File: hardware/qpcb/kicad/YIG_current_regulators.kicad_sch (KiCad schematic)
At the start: 19 parts, among them IC12 DAC8562TDGSR, J16 Conn_01x04, J17 Conn_01x04, Q7 NPN, Q8 NPN, U21 LT1632CS8#PBF, U22 LT1632CS8#PBF

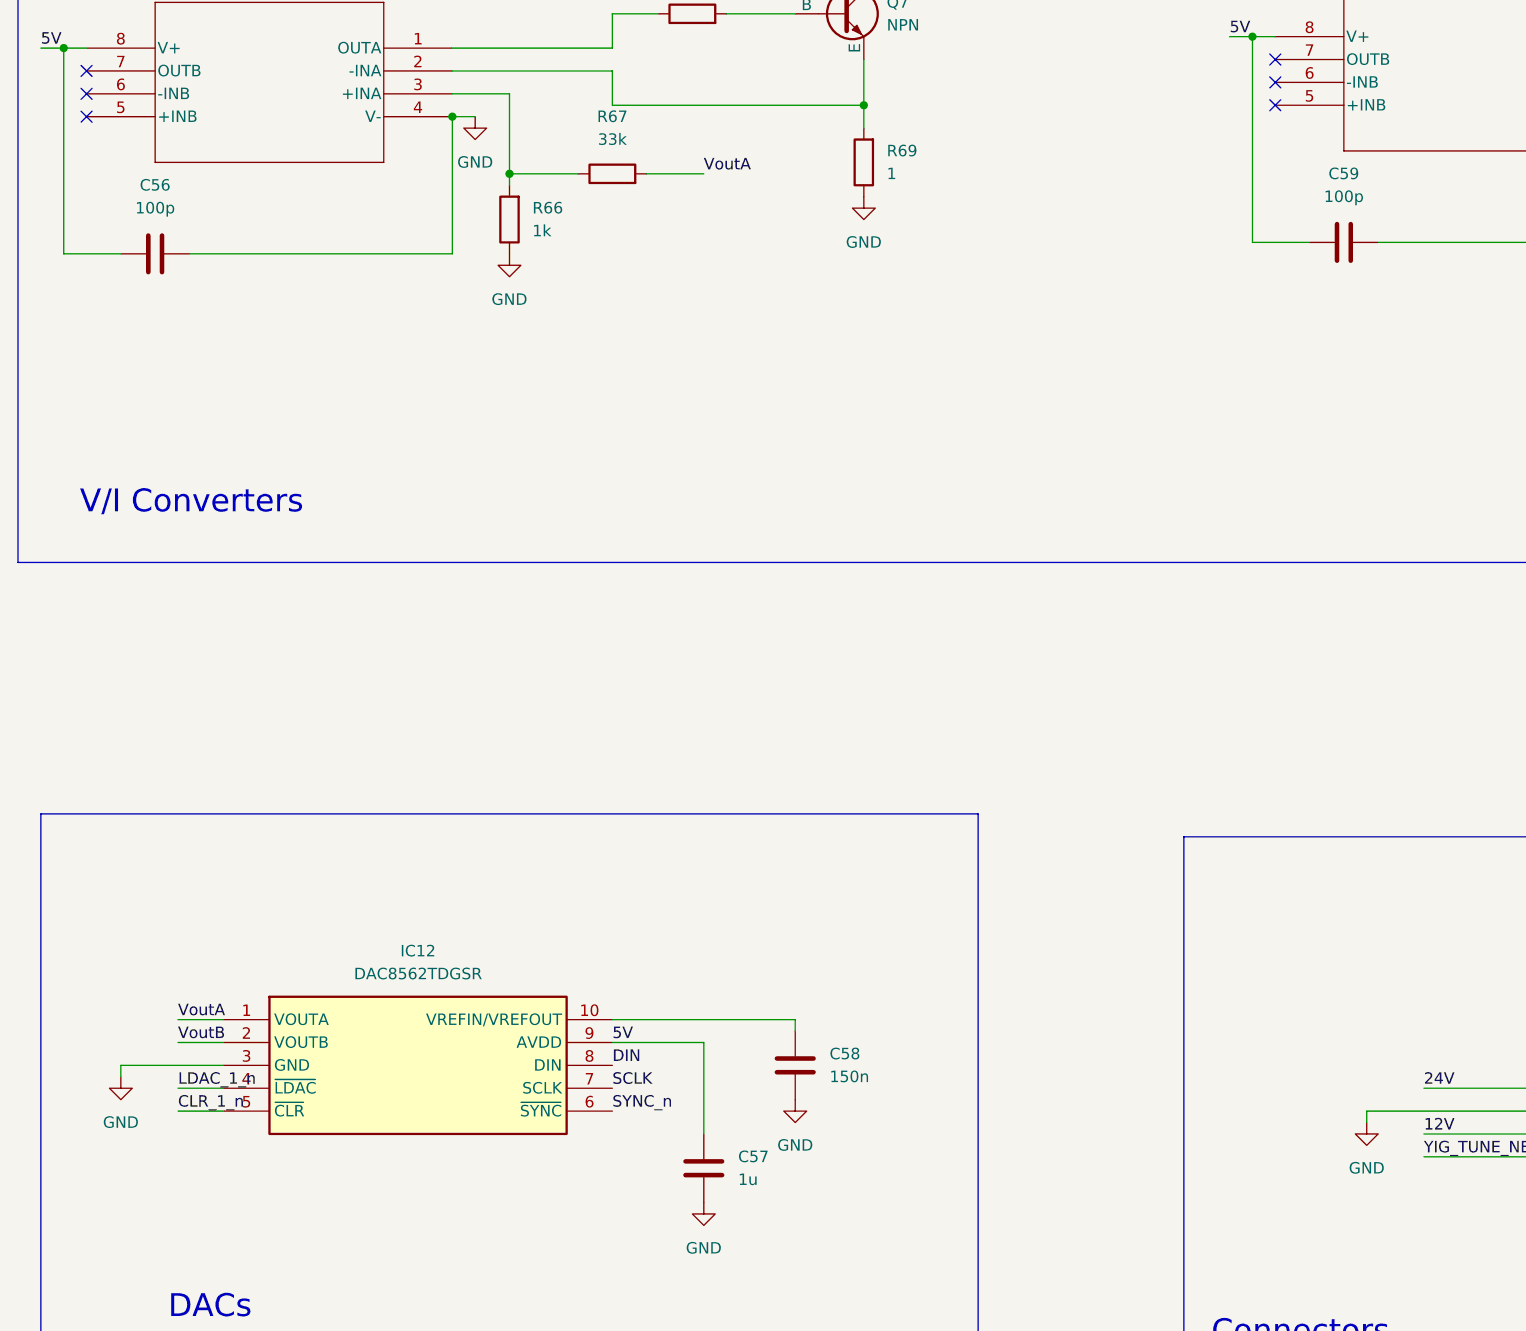
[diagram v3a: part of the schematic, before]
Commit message: Add final footprints of daughter boards, change components for -3v3 power supply line and placement almost finished
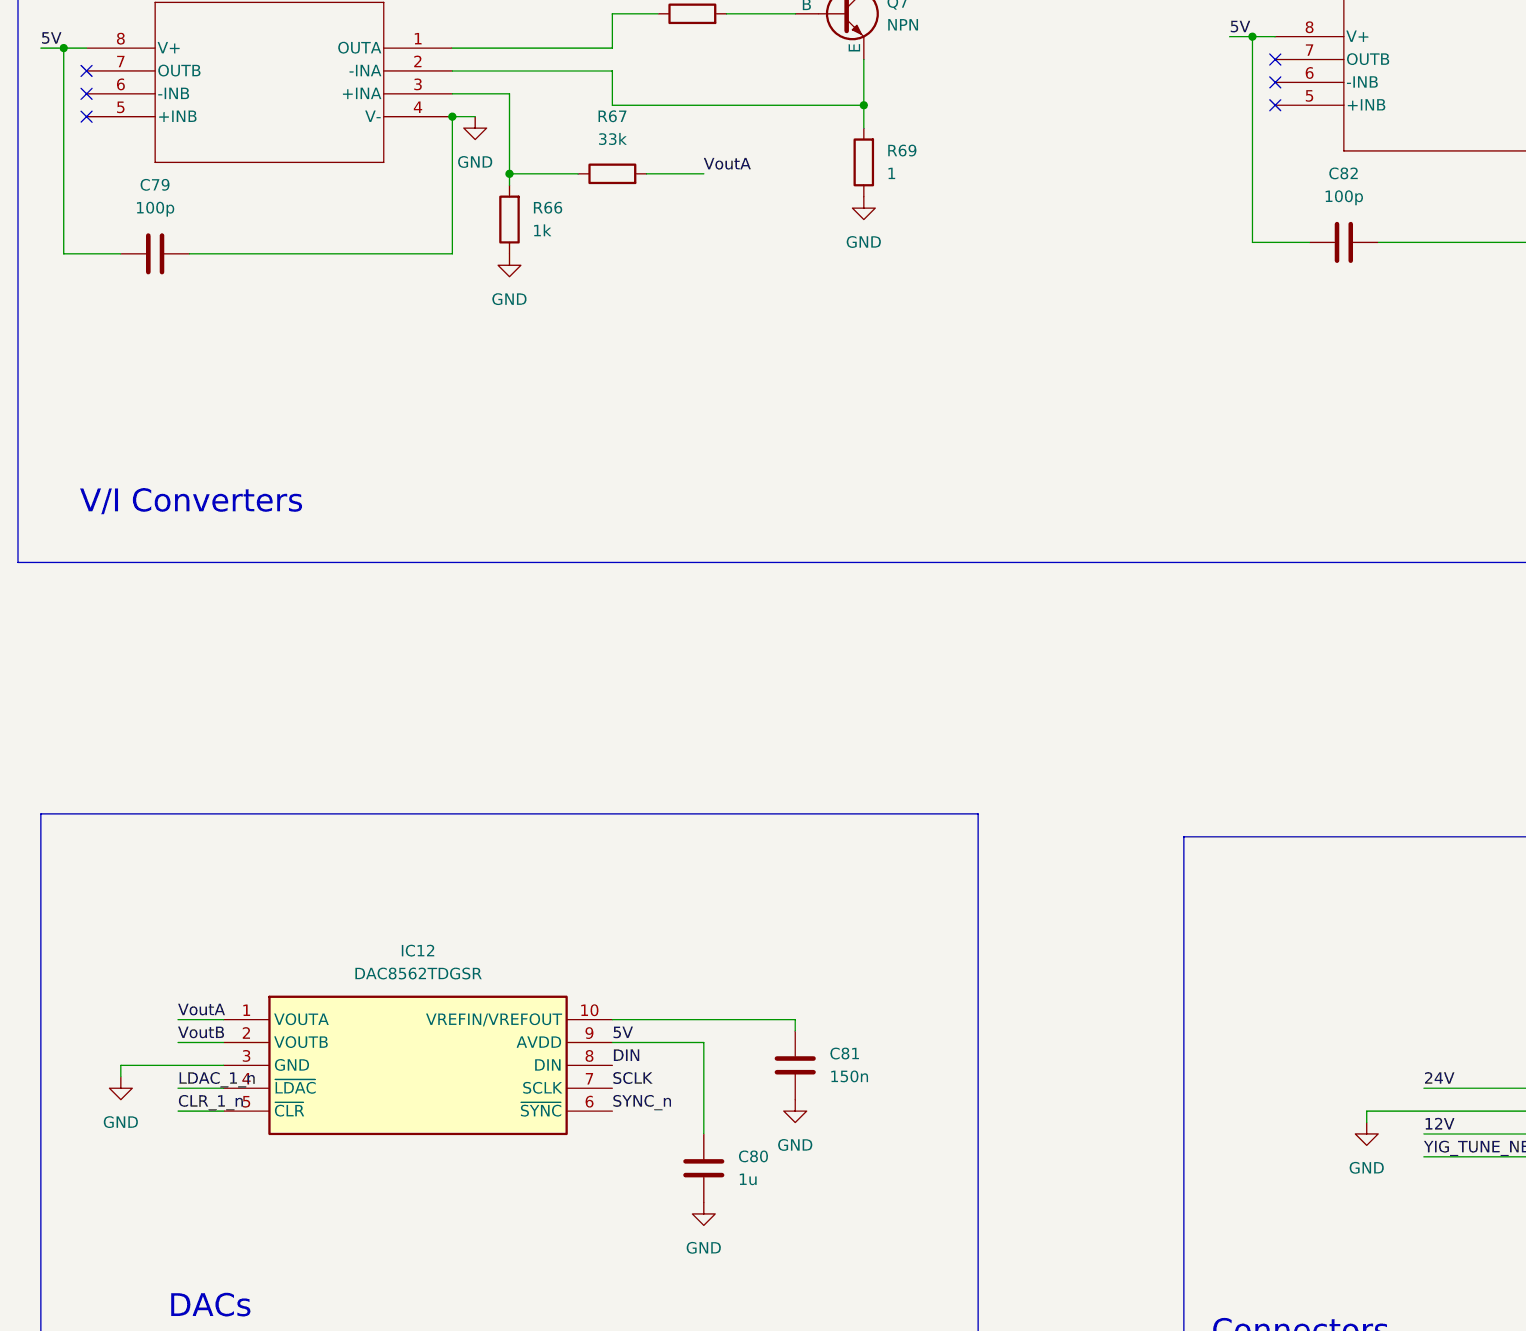
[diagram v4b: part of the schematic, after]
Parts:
- renumbered C56 to C79, C57 to C80, C58 to C81, C59 to C82
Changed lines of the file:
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@@
 		(dnp no)
 		(fields_autoplaced yes)
-		(property "Reference" "#PWR0120"
+		(property "Reference" "#PWR0145"
 			(at 204.47 74.93 0)
 			(effects
@@
 			(project "qpcb"
 				(path "/c131d68b-62f5-4c45-b130-1d10920b3403/0e1314fc-8bce-4819-a5af-1738951867e1"
-					(reference "#PWR0120")
+					(reference "#PWR0145")
 					(unit 1)
 				)
@@
 		(dnp no)
 		(fields_autoplaced yes)
-		(property "Reference" "C57"
+		(property "Reference" "C80"
 			(at 97.79 170.1799 0)
 			(effects
@@
 			(project "qpcb"
 				(path "/c131d68b-62f5-4c45-b130-1d10920b3403/0e1314fc-8bce-4819-a5af-1738951867e1"
-					(reference "C57")
+					(reference "C80")
 					(unit 1)
 				)
@@
 		(dnp no)
 		(fields_autoplaced yes)
-		(property "Reference" "C56"
+		(property "Reference" "C79"
 			(at 33.02 62.23 90)
 			(effects
@@
 			(project "qpcb"
 				(path "/c131d68b-62f5-4c45-b130-1d10920b3403/0e1314fc-8bce-4819-a5af-1738951867e1"
-					(reference "C56")
+					(reference "C79")
 					(unit 1)
 				)
@@
 		(dnp no)
 		(fields_autoplaced yes)
-		(property "Reference" "#PWR0118"
+		(property "Reference" "#PWR0143"
 			(at 167.64 172.72 0)
 			(effects
@@
 			(project "qpcb"
 				(path "/c131d68b-62f5-4c45-b130-1d10920b3403/0e1314fc-8bce-4819-a5af-1738951867e1"
-					(reference "#PWR0118")
+					(reference "#PWR0143")
 					(unit 1)
 				)
@@
 		(dnp no)
 		(fields_autoplaced yes)
-		(property "Reference" "C58"
+		(property "Reference" "C81"
 			(at 107.95 158.7499 0)
 			(effects
@@
 			(project "qpcb"
 				(path "/c131d68b-62f5-4c45-b130-1d10920b3403/0e1314fc-8bce-4819-a5af-1738951867e1"
-					(reference "C58")
+					(reference "C81")
 					(unit 1)
 				)
@@
 		(dnp no)
 		(fields_autoplaced yes)
-		(property "Reference" "#PWR0122"
+		(property "Reference" "#PWR0147"
 			(at 243.84 68.58 0)
 			(effects
@@
 			(project "qpcb"
 				(path "/c131d68b-62f5-4c45-b130-1d10920b3403/0e1314fc-8bce-4819-a5af-1738951867e1"
-					(reference "#PWR0122")
+					(reference "#PWR0147")
 					(unit 1)
 				)
@@
 		(dnp no)
 		(fields_autoplaced yes)
-		(property "Reference" "#PWR0117"
+		(property "Reference" "#PWR0142"
 			(at 111.76 69.85 0)
 			(effects
@@
 			(project "qpcb"
 				(path "/c131d68b-62f5-4c45-b130-1d10920b3403/0e1314fc-8bce-4819-a5af-1738951867e1"
-					(reference "#PWR0117")
+					(reference "#PWR0142")
 					(unit 1)
 				)
@@
 		(dnp no)
 		(fields_autoplaced yes)
-		(property "Reference" "C59"
+		(property "Reference" "C82"
 			(at 165.1 60.96 90)
 			(effects
@@
 			(project "qpcb"
 				(path "/c131d68b-62f5-4c45-b130-1d10920b3403/0e1314fc-8bce-4819-a5af-1738951867e1"
-					(reference "C59")
+					(reference "C82")
 					(unit 1)
 				)
@@
 		(dnp no)
 		(fields_autoplaced yes)
-		(property "Reference" "#PWR0114"
+		(property "Reference" "#PWR0139"
 			(at 72.39 76.2 0)
 			(effects
@@
 			(project "qpcb"
 				(path "/c131d68b-62f5-4c45-b130-1d10920b3403/0e1314fc-8bce-4819-a5af-1738951867e1"
-					(reference "#PWR0114")
+					(reference "#PWR0139")
 					(unit 1)
 				)
@@
 		(dnp no)
 		(fields_autoplaced yes)
-		(property "Reference" "#PWR0119"
+		(property "Reference" "#PWR0144"
 			(at 200.66 59.69 0)
 			(effects
@@
 			(project "qpcb"
 				(path "/c131d68b-62f5-4c45-b130-1d10920b3403/0e1314fc-8bce-4819-a5af-1738951867e1"
-					(reference "#PWR0119")
+					(reference "#PWR0144")
 					(unit 1)
 				)
@@
 		(dnp no)
 		(fields_autoplaced yes)
-		(property "Reference" "#PWR0115"
+		(property "Reference" "#PWR0140"
 			(at 93.98 181.61 0)
 			(effects
@@
 			(project "qpcb"
 				(path "/c131d68b-62f5-4c45-b130-1d10920b3403/0e1314fc-8bce-4819-a5af-1738951867e1"
-					(reference "#PWR0115")
+					(reference "#PWR0140")
 					(unit 1)
 				)
@@
 		(dnp no)
 		(fields_autoplaced yes)
-		(property "Reference" "#PWR0113"
+		(property "Reference" "#PWR0138"
 			(at 68.58 60.96 0)
 			(effects
@@
 			(project "qpcb"
 				(path "/c131d68b-62f5-4c45-b130-1d10920b3403/0e1314fc-8bce-4819-a5af-1738951867e1"
-					(reference "#PWR0113")
+					(reference "#PWR0138")
 					(unit 1)
 				)
@@
 		(dnp no)
 		(fields_autoplaced yes)
-		(property "Reference" "#PWR0112"
+		(property "Reference" "#PWR0137"
 			(at 29.21 167.64 0)
 			(effects
@@
 			(project "qpcb"
 				(path "/c131d68b-62f5-4c45-b130-1d10920b3403/0e1314fc-8bce-4819-a5af-1738951867e1"
-					(reference "#PWR0112")
+					(reference "#PWR0137")
 					(unit 1)
 				)
@@
 		(dnp no)
 		(fields_autoplaced yes)
-		(property "Reference" "#PWR0121"
+		(property "Reference" "#PWR0146"
 			(at 215.9 172.72 0)
 			(effects
@@
 			(project "qpcb"
 				(path "/c131d68b-62f5-4c45-b130-1d10920b3403/0e1314fc-8bce-4819-a5af-1738951867e1"
-					(reference "#PWR0121")
+					(reference "#PWR0146")
 					(unit 1)
 				)
@@
 		(dnp no)
 		(fields_autoplaced yes)
-		(property "Reference" "#PWR0116"
+		(property "Reference" "#PWR0141"
 			(at 104.14 170.18 0)
 			(effects
@@
 			(project "qpcb"
 				(path "/c131d68b-62f5-4c45-b130-1d10920b3403/0e1314fc-8bce-4819-a5af-1738951867e1"
-					(reference "#PWR0116")
-					(unit 1)
-				)
+					(reference "#PWR0141")
+					(unit 1)
+				)

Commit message: Add QPCB JLCPCB production files
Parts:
- C79, C82: LCSC (none) -> C2255672
- C81: LCSC (none) -> C2172092
- IC12: LCSC (none) -> C1554732
- J16, J17: LCSC (none) -> C3025061
- R69, R73: LCSC (none) -> C313850
- U21, U22: LCSC (none) -> C579789
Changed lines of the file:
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@@
+			)
+		)
+		(property "LCSC" "C313850"
+			(at 111.76 59.69 0)
+			(effects
+				(font
+					(size 1.27 1.27)
+				)
+				(hide yes)
 			)
 		)
@@
 			)
 		)
+		(property "LCSC" "C2255672"
+			(at 33.02 69.85 0)
+			(effects
+				(font
+					(size 1.27 1.27)
+				)
+				(hide yes)
+			)
+		)
 		(pin "1"
 		)
@@
 		)
 		(property "Mating Crimp" ""
+			(at 44.45 50.8 0)
+			(effects
+				(font
+					(size 1.27 1.27)
+				)
+				(hide yes)
+			)
+		)
+		(property "LCSC" "C579789"
 			(at 44.45 50.8 0)
 			(effects
@@
 			)
 		)
+		(property "LCSC" "C2172092"
+			(at 104.14 160.02 0)
+			(effects
+				(font
+					(size 1.27 1.27)
+				)
+				(hide yes)
+			)
+		)
 		(pin "1"
 		)
@@
 			)
 		)
+		(property "LCSC" "C3025061"
+			(at 243.84 165.1 0)
+			(effects
+				(font
+					(size 1.27 1.27)
+				)
+				(hide yes)
+			)
+		)
 		(pin "4"
 		)
@@
 			)
 		)
+		(property "LCSC" "C2255672"
+			(at 165.1 68.58 0)
+			(effects
+				(font
+					(size 1.27 1.27)
+				)
+				(hide yes)
+			)
+		)
 		(pin "1"
 		)
@@
 			)
 		)
+		(property "LCSC" "C579789"
+			(at 176.53 49.53 0)
+			(effects
+				(font
+					(size 1.27 1.27)
+				)
+				(hide yes)
+			)
+		)
 		(pin "3"
 		)
@@
 			)
 		)
+		(property "LCSC" "C313850"
+			(at 243.84 58.42 0)
+			(effects
+				(font
+					(size 1.27 1.27)
+				)
+				(hide yes)
+			)
+		)
 		(pin "2"
 		)
@@
 		)
 		(property "Mating Part" "538-47054-1000"
+			(at 195.58 165.1 0)
+			(effects
+				(font
+					(size 1.27 1.27)
+				)
+				(hide yes)
+			)
+		)
+		(property "LCSC" "C3025061"
 			(at 195.58 165.1 0)
 			(effects
@@
 			(at 62.23 160.02 0)
 			(effects
+				(font
+					(size 1.27 1.27)
+				)
+				(hide yes)
+			)
+		)
+		(property "LCSC" "C1554732"
+			(at 62.23 160.02 0)
+			(effects
